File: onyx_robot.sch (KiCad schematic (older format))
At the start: 30 parts, among them P1 EXT1, P2 EXT2, P3 READER, P4 FTDI, Q1 Q_NMOS_GSD, Q2 Q_NMOS_GSD, SW1 RESET, U1 ADP2301, U2 RELAY_SPDT, U3 ESP-12E

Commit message: Version 2
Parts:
- added R12, R13: 2K2, Resistors_SMD:R_0603, symbol R
- added R14: 10K, Resistors_SMD:R_0603, symbol R
- P1: value EXT1 -> POWER; footprint timhawes:Terminal_Block_5.08mm_x6 -> timhawes:Terminal_Block_5.08mm_x4; symbol CONN_01X06 -> CONN_01X04
- P2: value EXT2 -> INPUTS
- R5: value 10K -> 100R
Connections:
- net labels added: DOOR, PN532_RESET, SCL, SDA
- net labels removed: CLK, CS, DOOR_SENSE, MISO, MOSI, TAMPER
- wire segments 107 -> 108
- no-connect marks 6 -> 9

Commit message: Finished version 2
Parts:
- added D10, D11, D12, D3, D4, D5, D7, D8, D9: TVS, Diodes_SMD:SOD-523, symbol D_Schottky
- added D6: TVS, Diodes_SMD:SMA_Standard, symbol D_Schottky
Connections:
- wire segments 108 -> 127

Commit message: Revision 3
Off-the-shelf power supply module
5V supplied to NFC reader
Piezo improved
ESD protection removed to complexity
NC contact removed from relay
VCC removed from FTDI connector
Flyback diode added to relay output
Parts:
- removed C3: 0.1uF 6.3V, Capacitors_SMD:C_0603, symbol C
- removed D1: B230A, Diodes_SMD:Diode-SMA_Standard, symbol D_Schottky
- removed D10, D11, D12, D3, D4, D5, D7, D8, D9: TVS, Diodes_SMD:SOD-523, symbol D_Schottky
- removed D6: TVS, Diodes_SMD:SMA_Standard, symbol D_Schottky
- removed JP1: NO/NC, Pin_Headers:Pin_Header_Straight_1x03, symbol JUMPER3
- removed L1: 4.7μH 2A, timhawes:LPS6225, symbol INDUCTOR
- removed R1: 31K6 1%, Resistors_SMD:R_0603, symbol R
- removed R14: 10K, Resistors_SMD:R_0603, symbol R
- removed R2, R4: 10K2 1%, Resistors_SMD:R_0603, symbol R
- removed R3: 56K 1%, Resistors_SMD:R_0603, symbol R
- removed R5: 100R, Resistors_SMD:R_0603, symbol R
- removed U1: ADP2301, Housings_SOT-23_SOT-143_TSOT-6:SOT-23-6, symbol ADP2301
- added C3: 10uF 6.3V, Capacitor_SMD:C_0805_2012Metric, symbol Device:C
- added D1: D, Diode_SMD:D_SMA, symbol Device:D
- added R1: 1K, Resistor_SMD:R_0603_1608Metric, symbol Device:R
- added U1: R-78E5.0-1.0, Converter_DCDC:Converter_DCDC_RECOM_R-78E-0.5_THT, symbol Regulator_Switching:R-78E5.0-1.0
- added U4: SPX3819M5-L-3-3, Package_TO_SOT_SMD:SOT-23-5, symbol Regulator_Linear:SPX3819M5-L-3-3
- C1: footprint Capacitors_SMD:C_1206 -> Capacitor_SMD:C_0805_2012Metric; symbol C -> Device:C
- C2: value 22uF 6.3V -> 10uF 10V; footprint Capacitors_SMD:C_1206 -> Capacitor_SMD:C_0805_2012Metric; symbol C -> Device:C
- C4: footprint Capacitors_SMD:C_0603 -> Capacitor_SMD:C_0603_1608Metric; symbol C -> Device:C
- D2: footprint Diodes_SMD:Diode-SMA_Standard -> Diode_SMD:D_SMA; symbol D -> Device:D
- JP2: symbol JUMPER -> onyx_robot-rescue:JUMPER
- P1: symbol CONN_01X04 -> onyx_robot-rescue:CONN_01X04
- P2, P4: symbol CONN_01X06 -> onyx_robot-rescue:CONN_01X06
- P3: symbol CONN_01X08 -> onyx_robot-rescue:CONN_01X08
- Q1, Q2: symbol Q_NMOS_GSD -> Device:Q_NMOS_GSD
- R10, R11, R6, R7, R8, R9: footprint Resistors_SMD:R_0603 -> Resistor_SMD:R_0603_1608Metric; symbol R -> Device:R
- R12, R13: value 2K2 -> 4K7; footprint Resistors_SMD:R_0603 -> Resistor_SMD:R_0603_1608Metric; symbol R -> Device:R
- SW1: symbol SW_PUSH -> onyx_robot-rescue:SW_PUSH
- U2: footprint Relays_ThroughHole:Relay_SANYOU_SRD_Series_Form_C -> Relay_THT:Relay_SPDT_Omron-G5LE-1; symbol JS_RELAY -> timhawes:JS_RELAY
- U3: symbol ESP-12E -> onyx_robot-rescue:ESP-12E
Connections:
- net labels added: +5V
- wire segments 127 -> 121
- no-connect marks 9 -> 12

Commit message: Revision 4
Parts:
- added JP1: NO/NC, Connector_PinHeader_2.54mm:PinHeader_1x03_P2.54mm_Vertical, symbol Device:Jumper_NC_Dual
- JP2: footprint Pin_Headers:Pin_Header_Straight_1x02 -> Connector_PinHeader_2.54mm:PinHeader_1x02_P2.54mm_Vertical; symbol onyx_robot-rescue:JUMPER -> onyx_robot-rescue:JUMPER-onyx_robot-rescue
- P1: symbol onyx_robot-rescue:CONN_01X04 -> onyx_robot-rescue:CONN_01X04-onyx_robot-rescue
- P2, P4: symbol onyx_robot-rescue:CONN_01X06 -> onyx_robot-rescue:CONN_01X06-onyx_robot-rescue
- P3: symbol onyx_robot-rescue:CONN_01X08 -> onyx_robot-rescue:CONN_01X08-onyx_robot-rescue
- R14: renamed from R1; value 1K -> 10K
- SW1: symbol onyx_robot-rescue:SW_PUSH -> onyx_robot-rescue:SW_PUSH-onyx_robot-rescue
- U2: footprint Relay_THT:Relay_SPDT_Omron-G5LE-1 -> timhawes:JS_RELAY
- U3: symbol onyx_robot-rescue:ESP-12E -> onyx_robot-rescue:ESP-12E-onyx_robot-rescue
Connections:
- net +5V: now also R14.1
- net 12V_OUT: now also JP1.2; no longer U2.3
- net PIEZO: now also Q2.3 (D), R14.2; no longer R14.1
- net at U2.4: now also JP1.3
- new net: JP1.1, U2.3
- no-connect marks 12 -> 11
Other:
- moved on the sheet: R14
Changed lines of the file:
@@
 EESchema Schematic File Version 4
-LIBS:onyx_robot-cache
-EELAYER 29 0
+EELAYER 30 0
 EELAYER END
 $Descr A4 11693 8268
@@
 $EndDescr
 $Comp
-L onyx_robot-rescue:ESP-12E U3
+L onyx_robot-rescue:ESP-12E-onyx_robot-rescue U3
 U 1 1 55847B66
 P 8600 4275
@@
 $EndComp
 $Comp
-L onyx_robot-rescue:CONN_01X06 P4
+L onyx_robot-rescue:CONN_01X06-onyx_robot-rescue P4
 U 1 1 55847D6C
 P 4100 6525
@@
 $EndComp
 $Comp
-L onyx_robot-rescue:CONN_01X04 P1
+L onyx_robot-rescue:CONN_01X04-onyx_robot-rescue P1
 U 1 1 55847E1B
 P 1250 3700
@@
 $EndComp
 $Comp
-L onyx_robot-rescue:CONN_01X08 P3
+L onyx_robot-rescue:CONN_01X08-onyx_robot-rescue P3
 U 1 1 55847F14
 P 1250 6525
@@
 ADC
 $Comp
-L onyx_robot-rescue:SW_PUSH SW1
+L onyx_robot-rescue:SW_PUSH-onyx_robot-rescue SW1
 U 1 1 55848A10
 P 10100 2150
@@
 P 8000 1350
 F 0 "#PWR07" H 8000 1200 50  0001 C CNN
-F 1 "+3.3V" H 8000 1490 50  0000 C CNN
+F 1 "+3.3V" H 8000 1500 50  0000 C CNN
 F 2 "" H 8000 1350 60  0000 C CNN
 F 3 "" H 8000 1350 60  0000 C CNN
@@
 F 0 "U2" H 4400 4525 60  0000 C CNN
 F 1 "RELAY_SPDT" H 4400 4025 60  0000 C CNN
-F 2 "Relay_THT:Relay_SPDT_Omron-G5LE-1" H 3650 4475 60  0001 C CNN
+F 2 "timhawes:JS_RELAY" H 3650 4475 60  0001 C CNN
 F 3 "" H 3650 4475 60  0000 C CNN
 	1    4400 4275
@@
 Text GLabel 3475 4875 0    60   Input ~ 0
 RELAY
-Text GLabel 4950 4425 2    60   Input ~ 0
+Text GLabel 5100 4725 3    60   Input ~ 0
 12V_OUT
 Text GLabel 1775 5100 2    60   Input ~ 0
@@
 PN532_RESET
 $Comp
-L onyx_robot-rescue:CONN_01X06 P2
+L onyx_robot-rescue:CONN_01X06-onyx_robot-rescue P2
 U 1 1 5585E73E
 P 1250 4950
@@
 	1    0    0    -1
 $EndComp
-Text GLabel 8825 1800 2    60   Input ~ 0
+Text GLabel 8650 1825 2    60   Input ~ 0
 PIEZO
 $Comp
@@
 GPIO0 LOW = Bootloader\nGPIO0 HIGH = Runtime
 $Comp
-L onyx_robot-rescue:JUMPER JP2
+L onyx_robot-rescue:JUMPER-onyx_robot-rescue JP2
 U 1 1 558E08A0
 P 8000 2550
 F 0 "JP2" H 8000 2700 50  0000 C CNN
 F 1 "BOOT" H 8000 2470 50  0000 C CNN
-F 2 "Pin_Headers:Pin_Header_Straight_1x02" H 8000 2550 60  0001 C CNN
+F 2 "Connector_PinHeader_2.54mm:PinHeader_1x02_P2.54mm_Vertical" H 8000 2550 60  0001 C CNN
 F 3 "" H 8000 2550 60  0000 C CNN
 	1    8000 2550
@@
 	4875 4275 4700 4275
 Wire Wire Line
-	4700 4425 4950 4425
+	4700 4425 4850 4425
 Wire Wire Line
 	1400 1375 1575 1375
@@
 Wire Wire Line
 	1450 3850 2025 3850
-Wire Wire Line
-	8350 1800 8450 1800
 Wire Wire Line
 	1450 3550 1500 3550
@@
 	1575 2500 1575 2625
 Wire Wire Line
-	8000 1350 8000 1650
-Wire Wire Line
-	8350 1800 8350 1900
-$Comp
-L Device:R R1
+	8350 1725 8350 1825
+$Comp
+L Device:R R14
 U 1 1 5D48E402
-P 8600 1800
-F 0 "R1" V 8500 1800 50  0000 C CNN
-F 1 "1K" V 8600 1800 50  0000 C CNN
-F 2 "Resistor_SMD:R_0603_1608Metric" V 8530 1800 50  0001 C CNN
-F 3 "~" H 8600 1800 50  0001 C CNN
-	1    8600 1800
-	0    1    1    0
-$EndComp
-Wire Wire Line
-	8750 1800 8825 1800
+P 8350 1575
+F 0 "R14" V 8250 1575 50  0000 C CNN
+F 1 "10K" V 8350 1575 50  0000 C CNN
+F 2 "Resistor_SMD:R_0603_1608Metric" V 8280 1575 50  0001 C CNN
+F 3 "~" H 8350 1575 50  0001 C CNN
+	1    8350 1575
+	1    0    0    -1
+$EndComp
+Wire Wire Line
+	8350 1825 8650 1825
 $Comp
 L Regulator_Switching:R-78E5.0-1.0 U1
@@
 Wire Wire Line
 	2775 1475 2775 1750
-NoConn ~ 4700 4125
 Wire Wire Line
 	6100 6650 6100 6750
@@
 Wire Wire Line
 	1450 4700 1775 4700
+Wire Wire Line
+	8350 1350 8350 1425
+Connection ~ 8350 1825
+Wire Wire Line
+	8350 1825 8350 1900
+Wire Wire Line
+	8000 1350 8000 1650
+$Comp
+L power:+5V #PWR0105
+U 1 1 5F0F5490
+P 8350 1350
+F 0 "#PWR0105" H 8350 1200 50  0001 C CNN
+F 1 "+5V" H 8350 1500 50  0000 C CNN
+F 2 "" H 8350 1350 50  0001 C CNN
+F 3 "" H 8350 1350 50  0001 C CNN
+	1    8350 1350
+	1    0    0    -1
+$EndComp
+$Comp
+L Device:Jumper_NC_Dual JP1
+U 1 1 5F109367
+P 5100 4425
+F 0 "JP1" H 5225 4325 50  0000 C CNN
+F 1 "NO/NC" H 5100 4573 50  0000 C CNN
+F 2 "Connector_PinHeader_2.54mm:PinHeader_1x03_P2.54mm_Vertical" H 5100 4425 50  0001 C CNN
+F 3 "~" H 5100 4425 50  0001 C CNN
+	1    5100 4425
+	1    0    0    -1
+$EndComp
+Wire Wire Line
+	5100 4525 5100 4725
+Wire Wire Line
+	4700 4125 5450 4125
+Wire Wire Line
+	5450 4125 5450 4425
+Wire Wire Line
+	5450 4425 5350 4425
 $EndSCHEMATC

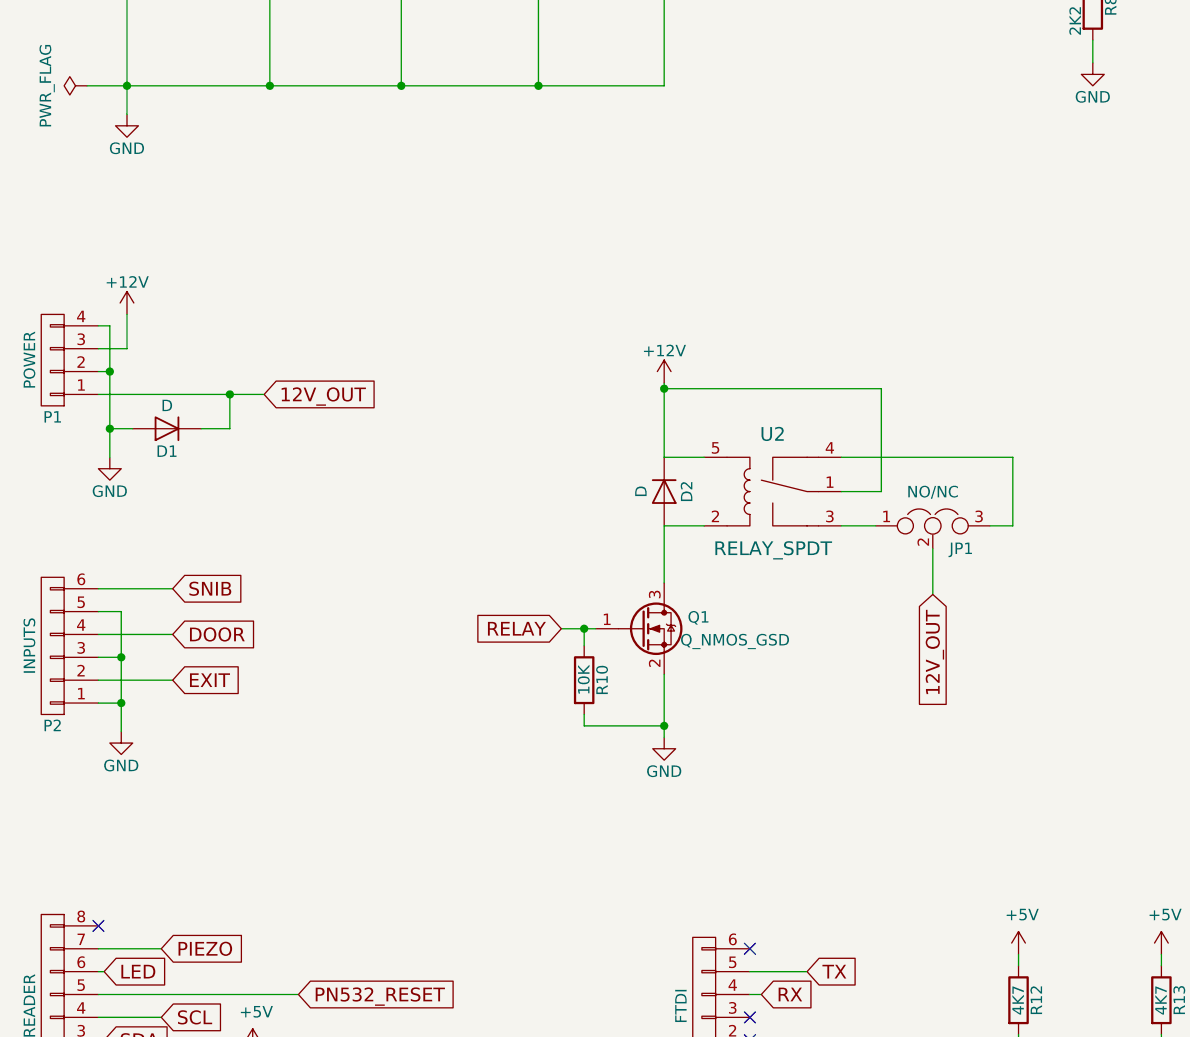
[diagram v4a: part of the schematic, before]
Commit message: No volt relay option
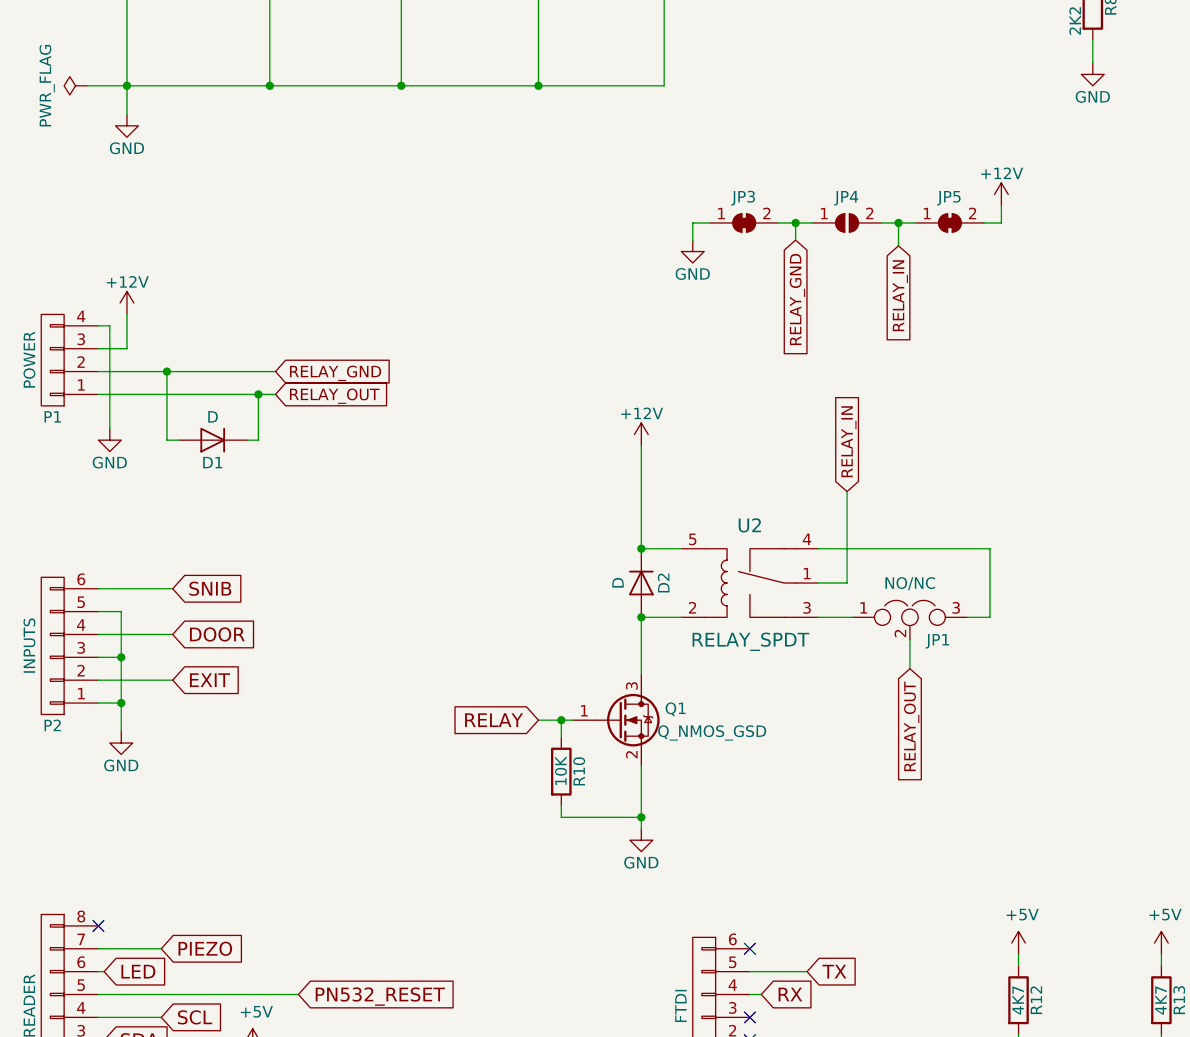
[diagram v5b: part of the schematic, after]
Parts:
- added JP3, JP5: SolderJumper_2_Bridged, Jumper:SolderJumper-2_P1.3mm_Bridged_RoundedPad1.0x1.5mm, symbol Jumper:SolderJumper_2_Bridged
- added JP4: SolderJumper_2_Open, Jumper:SolderJumper-2_P1.3mm_Open_RoundedPad1.0x1.5mm, symbol Jumper:SolderJumper_2_Open
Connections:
- net +12V: now also JP5.2 (B); no longer U2.1
- net GND: now also JP3.1 (A); no longer D1.2 (A), P1.2 (P2)
- net 12V_OUT renamed RELAY_OUT
- new net RELAY_GND: D1.2 (A), JP3.2 (B), JP4.1 (A), P1.2 (P2)
- new net RELAY_IN: JP4.2 (B), JP5.1 (A), U2.1
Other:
- moved on the sheet: D1, D2, JP1, Q1, R10, U2
